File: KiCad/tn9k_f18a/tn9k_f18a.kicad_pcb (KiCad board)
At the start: 2 copper layers, 32 x 94.9 mm, 27 parts, among them J2 VGA, J3 Tang Nano 9k, J4 TN9k/2, J5 VGA, J6 VGA, U1 1G08, U4 74LCX16245

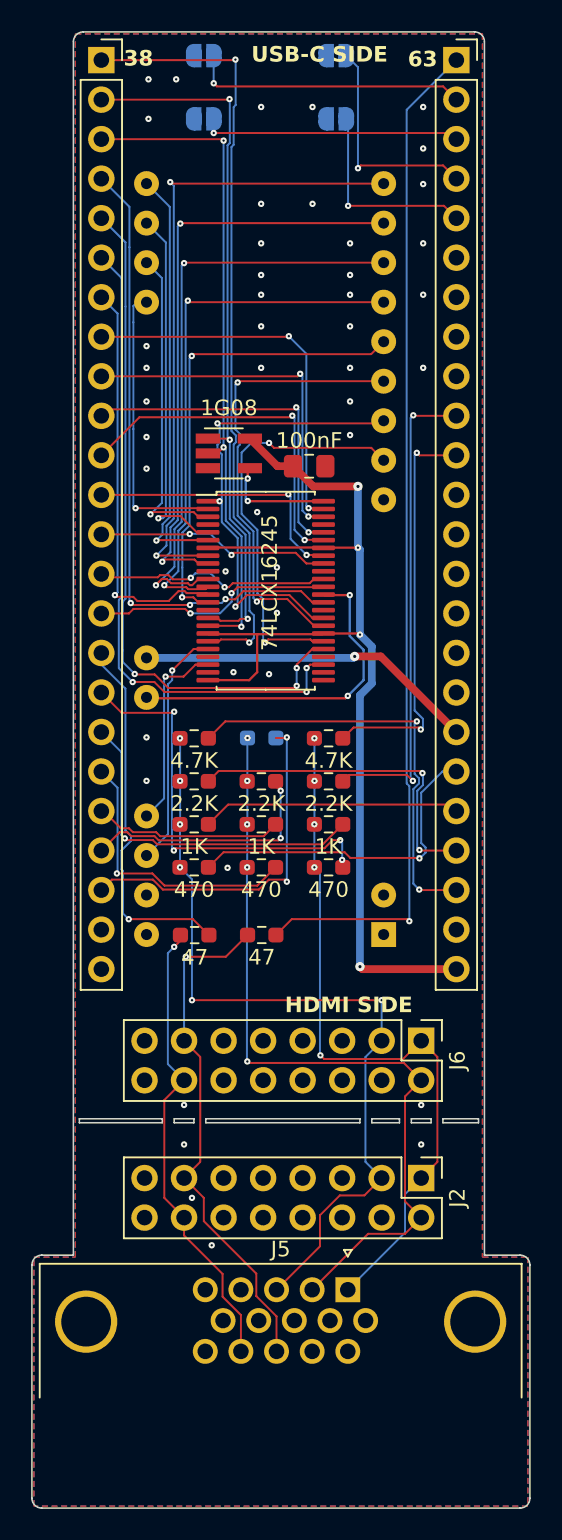
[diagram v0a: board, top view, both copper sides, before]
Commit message: silkscreen tweaks
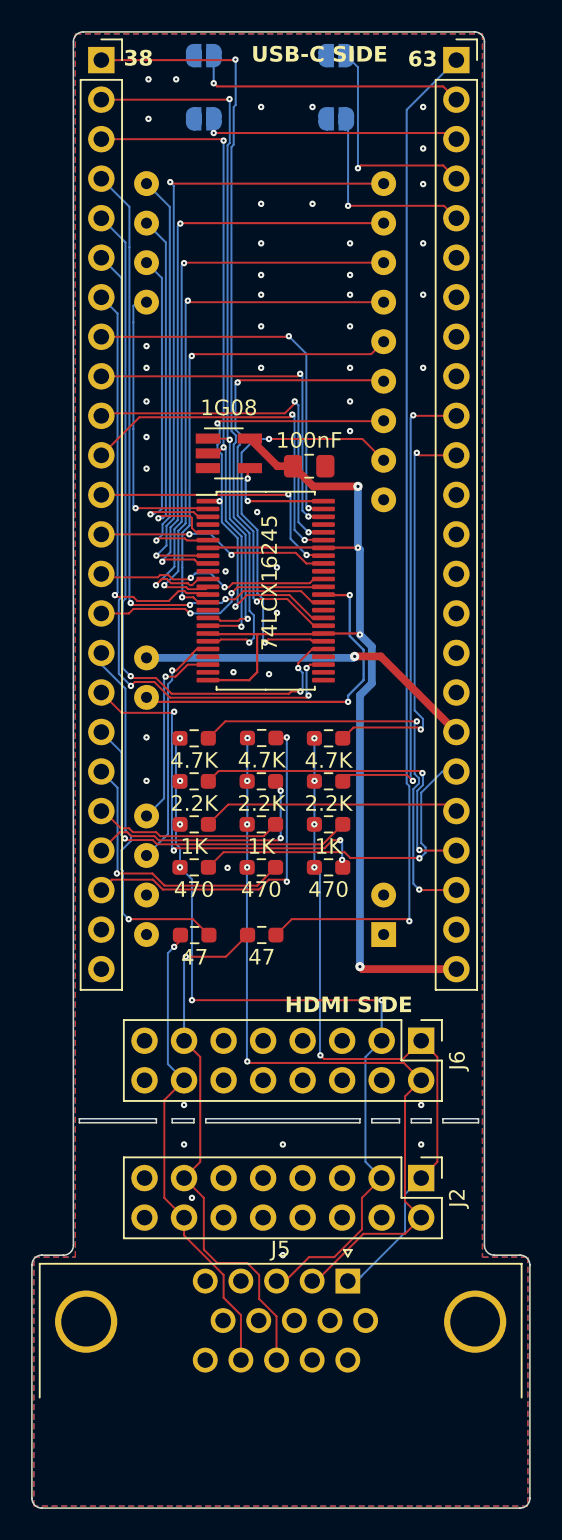
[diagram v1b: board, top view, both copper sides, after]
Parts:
- R5: moved to F.Cu
- turned R5 to 0 degrees
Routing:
- net HSYNC: track 33.3 -> 35.0 mm
- net BLUE: track 52.6 -> 54.2 mm
- net CPUCLK_3V3: track 44.7 -> 45.8 mm
- net GROMCLK_3V3: track 42.4 -> 43.4 mm
- net RED: track 46.5 -> 47.4 mm
- net VSYNC: track 30.1 -> 30.6 mm
- net CD2_3V3: track 22.1 -> 22.6 mm
- net GND: vias 45 -> 46
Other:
- outline, holes or cut-outs redrawn
- board text added: "TANG NANO 9K F18A 2023 Luis Antoniosi, Hans Hübner https://github.com/lfantoniosi/tn9k_f18a"
- board text removed: "TANG NANO 9K F18A 2023 LUIS ANTONIOSI"
